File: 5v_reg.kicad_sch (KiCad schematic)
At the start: 19 parts, among them U3 IR3899A

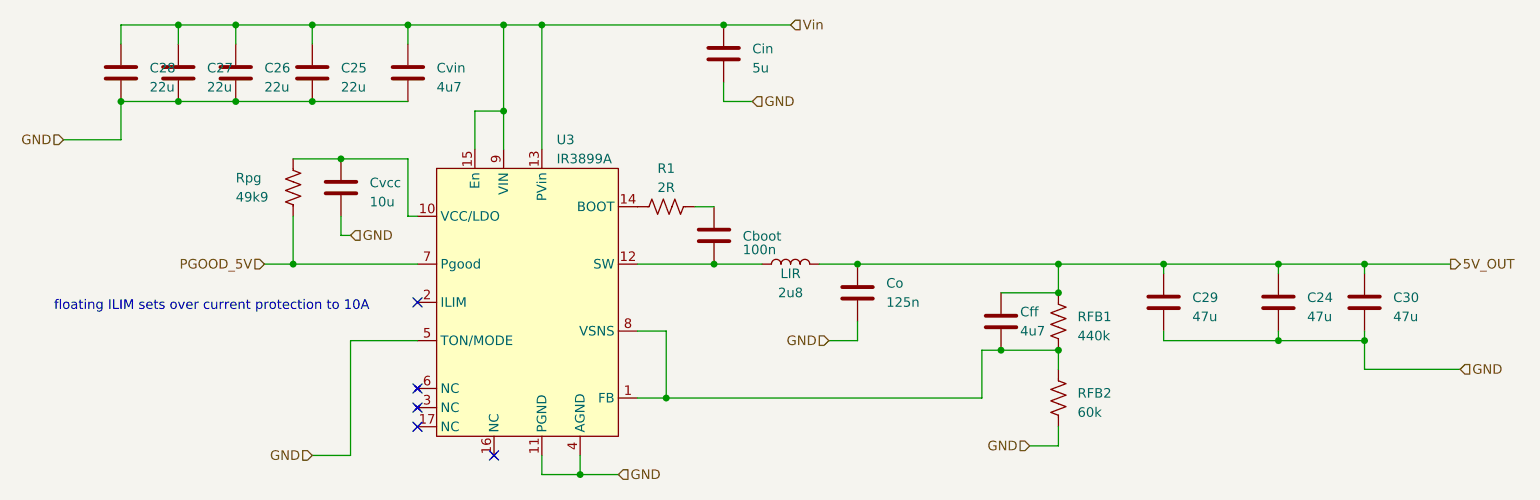
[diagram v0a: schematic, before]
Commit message: Fixed reference designators
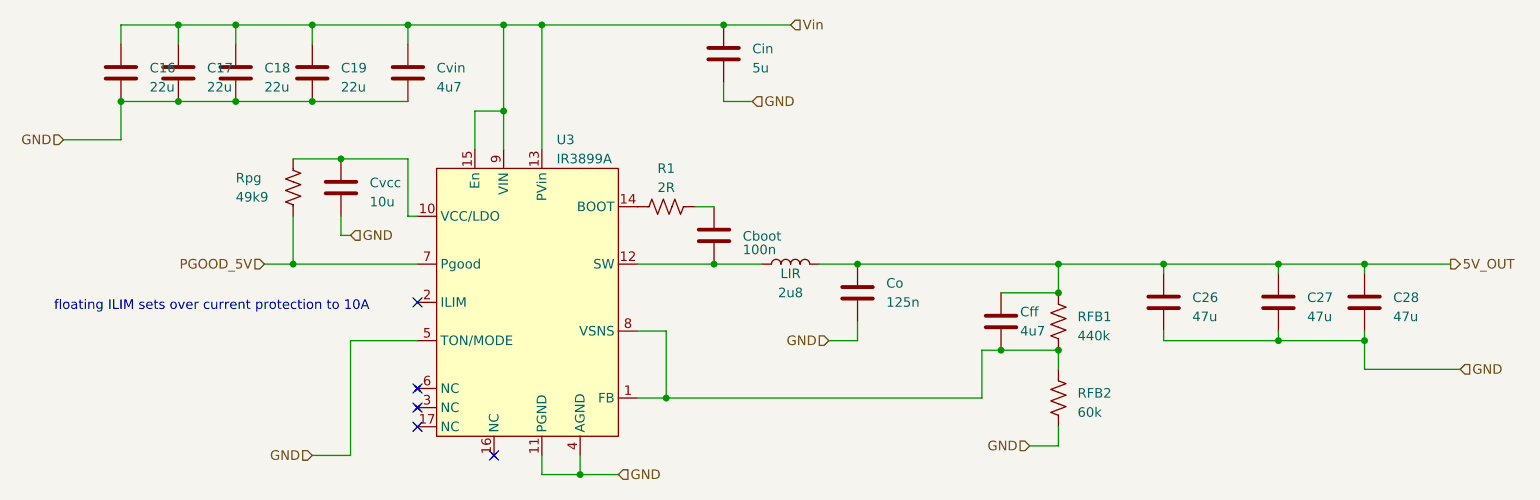
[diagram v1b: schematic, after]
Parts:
- renumbered C28 to C16, C27 to C17, C26 to C18, C25 to C19, C29 to C26, C24 to C27, C30 to C28
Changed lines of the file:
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@@
         )
         (path "/530b9f5d-4c5f-47a4-a889-3cce870d311f/66b48989-026d-4927-b86c-76e19138a6ff"
-          (reference "C20") (unit 1)
+          (reference "C22") (unit 1)
         )
       )
@@
   (symbol (lib_id "Device:C") (at 87.63 66.04 0) (unit 1)
     (in_bom yes) (on_board yes) (dnp no) (fields_autoplaced)
-    (property "Reference" "C27" (at 91.44 65.405 0)
+    (property "Reference" "C17" (at 91.44 65.405 0)
       (effects (font (size 1.27 1.27)) (justify left))
     )
@@
       (project "crush-power-board"
         (path "/530b9f5d-4c5f-47a4-a889-3cce870d311f/66b48989-026d-4927-b86c-76e19138a6ff"
-          (reference "C27") (unit 1)
+          (reference "C17") (unit 1)
         )
       )
@@
   (symbol (lib_id "Device:C") (at 105.41 66.04 0) (unit 1)
     (in_bom yes) (on_board yes) (dnp no) (fields_autoplaced)
-    (property "Reference" "C25" (at 109.22 65.405 0)
+    (property "Reference" "C19" (at 109.22 65.405 0)
       (effects (font (size 1.27 1.27)) (justify left))
     )
@@
       (project "crush-power-board"
         (path "/530b9f5d-4c5f-47a4-a889-3cce870d311f/66b48989-026d-4927-b86c-76e19138a6ff"
-          (reference "C25") (unit 1)
+          (reference "C19") (unit 1)
         )
       )
@@
         )
         (path "/530b9f5d-4c5f-47a4-a889-3cce870d311f/66b48989-026d-4927-b86c-76e19138a6ff"
+          (reference "C25") (unit 1)
+        )
+      )
+    )
+  )
+  (symbol (lib_id "Device:C") (at 160.02 63.5 0) (unit 1)
+    (in_bom yes) (on_board yes) (dnp no) (fields_autoplaced)
+    (property "Reference" "Cin" (at 163.83 62.865 0)
+      (effects (font (size 1.27 1.27)) (justify left))
+    )
+    (property "Value" "5u" (at 163.83 65.405 0)
+      (effects (font (size 1.27 1.27)) (justify left))
+    )
+    (property "Footprint" "" (at 160.9852 67.31 0)
+      (effects (font (size 1.27 1.27)) hide)
+    )
+    (property "Datasheet" "~" (at 160.02 63.5 0)
+      (effects (font (size 1.27 1.27)) hide)
+    )
+    (pin "1")
+    (pin "2")
+    (instances
+      (project "crush-power-board"
+        (path "/530b9f5d-4c5f-47a4-a889-3cce870d311f"
+          (reference "Cin") (unit 1)
+        )
+        (path "/530b9f5d-4c5f-47a4-a889-3cce870d311f/66b48989-026d-4927-b86c-76e19138a6ff"
           (reference "C23") (unit 1)
         )
@@
     )
   )
-  (symbol (lib_id "Device:C") (at 160.02 63.5 0) (unit 1)
-    (in_bom yes) (on_board yes) (dnp no) (fields_autoplaced)
-    (property "Reference" "Cin" (at 163.83 62.865 0)
-      (effects (font (size 1.27 1.27)) (justify left))
-    )
-    (property "Value" "5u" (at 163.83 65.405 0)
-      (effects (font (size 1.27 1.27)) (justify left))
-    )
-    (property "Footprint" "" (at 160.9852 67.31 0)
-      (effects (font (size 1.27 1.27)) hide)
-    )
-    (property "Datasheet" "~" (at 160.02 63.5 0)
-      (effects (font (size 1.27 1.27)) hide)
-    )
-    (pin "1")
-    (pin "2")
-    (instances
-      (project "crush-power-board"
-        (path "/530b9f5d-4c5f-47a4-a889-3cce870d311f"
-          (reference "Cin") (unit 1)
-        )
-        (path "/530b9f5d-4c5f-47a4-a889-3cce870d311f/66b48989-026d-4927-b86c-76e19138a6ff"
-          (reference "C21") (unit 1)
-        )
-      )
-    )
-  )
   (symbol (lib_id "Device:C") (at 218.44 96.52 0) (unit 1)
     (in_bom yes) (on_board yes) (dnp no) (fields_autoplaced)
-    (property "Reference" "C29" (at 222.25 95.885 0)
+    (property "Reference" "C26" (at 222.25 95.885 0)
       (effects (font (size 1.27 1.27)) (justify left))
     )
@@
       (project "crush-power-board"
         (path "/530b9f5d-4c5f-47a4-a889-3cce870d311f/66b48989-026d-4927-b86c-76e19138a6ff"
-          (reference "C29") (unit 1)
+          (reference "C26") (unit 1)
         )
       )
@@
   (symbol (lib_id "Device:C") (at 95.25 66.04 0) (unit 1)
     (in_bom yes) (on_board yes) (dnp no) (fields_autoplaced)
-    (property "Reference" "C26" (at 99.06 65.405 0)
+    (property "Reference" "C18" (at 99.06 65.405 0)
       (effects (font (size 1.27 1.27)) (justify left))
     )
@@
       (project "crush-power-board"
         (path "/530b9f5d-4c5f-47a4-a889-3cce870d311f/66b48989-026d-4927-b86c-76e19138a6ff"
-          (reference "C26") (unit 1)
+          (reference "C18") (unit 1)
         )
       )
@@
         )
         (path "/530b9f5d-4c5f-47a4-a889-3cce870d311f/66b48989-026d-4927-b86c-76e19138a6ff"
-          (reference "R1") (unit 1)
+          (reference "R16") (unit 1)
         )
       )
@@
         )
         (path "/530b9f5d-4c5f-47a4-a889-3cce870d311f/66b48989-026d-4927-b86c-76e19138a6ff"
-          (reference "C19") (unit 1)
+          (reference "C21") (unit 1)
         )
       )
@@
         )
         (path "/530b9f5d-4c5f-47a4-a889-3cce870d311f/66b48989-026d-4927-b86c-76e19138a6ff"
-          (reference "U2") (unit 1)
+          (reference "U3") (unit 1)
         )
       )
@@
         )
         (path "/530b9f5d-4c5f-47a4-a889-3cce870d311f/66b48989-026d-4927-b86c-76e19138a6ff"
-          (reference "R23") (unit 1)
+          (reference "R17") (unit 1)
         )
       )
@@
   (symbol (lib_id "Device:C") (at 233.68 96.52 0) (unit 1)
     (in_bom yes) (on_board yes) (dnp no) (fields_autoplaced)
-    (property "Reference" "C24" (at 237.49 95.885 0)
+    (property "Reference" "C27" (at 237.49 95.885 0)
       (effects (font (size 1.27 1.27)) (justify left))
     )
@@
       (project "crush-power-board"
         (path "/530b9f5d-4c5f-47a4-a889-3cce870d311f/66b48989-026d-4927-b86c-76e19138a6ff"
-          (reference "C24") (unit 1)
+          (reference "C27") (unit 1)
         )
       )
@@
         )
         (path "/530b9f5d-4c5f-47a4-a889-3cce870d311f/66b48989-026d-4927-b86c-76e19138a6ff"
-          (reference "R24") (unit 1)
+          (reference "R18") (unit 1)
         )
       )
@@
   (symbol (lib_id "Device:C") (at 245.11 96.52 0) (unit 1)
     (in_bom yes) (on_board yes) (dnp no) (fields_autoplaced)
-    (property "Reference" "C30" (at 248.92 95.885 0)
+    (property "Reference" "C28" (at 248.92 95.885 0)
       (effects (font (size 1.27 1.27)) (justify left))
     )
@@
       (project "crush-power-board"
         (path "/530b9f5d-4c5f-47a4-a889-3cce870d311f/66b48989-026d-4927-b86c-76e19138a6ff"
-          (reference "C30") (unit 1)
+          (reference "C28") (unit 1)
         )
       )
@@
         )
         (path "/530b9f5d-4c5f-47a4-a889-3cce870d311f/66b48989-026d-4927-b86c-76e19138a6ff"
-          (reference "C22") (unit 1)
+          (reference "C24") (unit 1)
         )
       )
@@
         )
         (path "/530b9f5d-4c5f-47a4-a889-3cce870d311f/66b48989-026d-4927-b86c-76e19138a6ff"
-          (reference "C18") (unit 1)
+          (reference "C20") (unit 1)
         )
       )
@@
         )
         (path "/530b9f5d-4c5f-47a4-a889-3cce870d311f/66b48989-026d-4927-b86c-76e19138a6ff"
-          (reference "L4") (unit 1)
+          (reference "L3") (unit 1)
         )
       )
@@
   (symbol (lib_id "Device:C") (at 80.01 66.04 0) (unit 1)
     (in_bom yes) (on_board yes) (dnp no) (fields_autoplaced)
-    (property "Reference" "C28" (at 83.82 65.405 0)
+    (property "Reference" "C16" (at 83.82 65.405 0)
       (effects (font (size 1.27 1.27)) (justify left))
     )
@@
       (project "crush-power-board"
         (path "/530b9f5d-4c5f-47a4-a889-3cce870d311f/66b48989-026d-4927-b86c-76e19138a6ff"
-          (reference "C28") (unit 1)
+          (reference "C16") (unit 1)
         )
       )
@@
         )
         (path "/530b9f5d-4c5f-47a4-a889-3cce870d311f/66b48989-026d-4927-b86c-76e19138a6ff"
-          (reference "R22") (unit 1)
-        )
-      )
+          (reference "R15") (unit 1)
+        )
+      )
